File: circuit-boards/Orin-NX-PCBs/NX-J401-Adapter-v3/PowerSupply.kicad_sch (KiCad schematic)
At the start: 23 parts, among them Q4 CSD16322Q5, Q5 SI4483ADY-T1-GE3, U2 LM3478MA

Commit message: Updated diff pairs and power supply layout
Signed-off-by: Scott <sgberman1@gmail.com>
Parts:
- renumbered C5 to C4, C13 to C5, C6 to C8, D3 to D1, R2 to R1, R8 to R4, R5 to R7, R6 to R8, U2 to U1
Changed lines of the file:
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@@
 	(title_block
 		(title "NX J401 Adapter")
-		(date "2024-08-05")
+		(date "2024-08-10")
 		(rev "3")
 		(company "971 Spartan Robotics")
@@
 		(on_board yes)
 		(dnp no)
-		(property "Reference" "R5"
+		(property "Reference" "R7"
 			(at 95.25 105.41 0)
 			(effects
@@
 			(project "NX-J401-Adapter"
 				(path "/cc31ce4b-09ab-4aea-a1d3-ed84696ba658/584f7d71-5922-4ce5-8f88-d664ca9e2a8c"
-					(reference "R5")
+					(reference "R7")
 					(unit 1)
 				)
@@
 			(project "NX-J401-Adapter"
 				(path "/cc31ce4b-09ab-4aea-a1d3-ed84696ba658/584f7d71-5922-4ce5-8f88-d664ca9e2a8c"
-					(reference "R9")
+					(reference "R6")
 					(unit 1)
 				)
@@
 			(project "NX-J401-Adapter"
 				(path "/cc31ce4b-09ab-4aea-a1d3-ed84696ba658/584f7d71-5922-4ce5-8f88-d664ca9e2a8c"
-					(reference "C7")
+					(reference "C3")
 					(unit 1)
 				)
@@
 			(project "NX-J401-Adapter"
 				(path "/cc31ce4b-09ab-4aea-a1d3-ed84696ba658/584f7d71-5922-4ce5-8f88-d664ca9e2a8c"
-					(reference "R3")
+					(reference "R5")
 					(unit 1)
 				)
@@
 			(project "NX-J401-Adapter"
 				(path "/cc31ce4b-09ab-4aea-a1d3-ed84696ba658/584f7d71-5922-4ce5-8f88-d664ca9e2a8c"
-					(reference "C11")
+					(reference "C7")
 					(unit 1)
 				)
@@
 			(project "NX-J401-Adapter"
 				(path "/cc31ce4b-09ab-4aea-a1d3-ed84696ba658/584f7d71-5922-4ce5-8f88-d664ca9e2a8c"
-					(reference "R4")
+					(reference "R2")
 					(unit 1)
 				)
@@
 		(on_board yes)
 		(dnp no)
-		(property "Reference" "C5"
+		(property "Reference" "C4"
 			(at 149.86 97.79 0)
 			(effects
@@
 			(project "NX-J401-Adapter"
 				(path "/cc31ce4b-09ab-4aea-a1d3-ed84696ba658/584f7d71-5922-4ce5-8f88-d664ca9e2a8c"
-					(reference "C5")
+					(reference "C4")
 					(unit 1)
 				)
@@
 		(dnp no)
 		(fields_autoplaced yes)
-		(property "Reference" "C13"
+		(property "Reference" "C5"
 			(at 130.81 98.425 0)
 			(effects
@@
 			(project "NX-J401-Adapter"
 				(path "/cc31ce4b-09ab-4aea-a1d3-ed84696ba658/584f7d71-5922-4ce5-8f88-d664ca9e2a8c"
-					(reference "C13")
+					(reference "C5")
 					(unit 1)
 				)
@@
 			(project "NX-J401-Adapter"
 				(path "/cc31ce4b-09ab-4aea-a1d3-ed84696ba658/584f7d71-5922-4ce5-8f88-d664ca9e2a8c"
-					(reference "D5")
+					(reference "D2")
 					(unit 1)
 				)
@@
 		(on_board yes)
 		(dnp no)
-		(property "Reference" "R8"
+		(property "Reference" "R4"
 			(at 284.48 116.84 0)
 			(effects
@@
 			(project "NX-J401-Adapter"
 				(path "/cc31ce4b-09ab-4aea-a1d3-ed84696ba658/584f7d71-5922-4ce5-8f88-d664ca9e2a8c"
-					(reference "R8")
+					(reference "R4")
 					(unit 1)
 				)
@@
 			(project "NX-J401-Adapter"
 				(path "/cc31ce4b-09ab-4aea-a1d3-ed84696ba658/584f7d71-5922-4ce5-8f88-d664ca9e2a8c"
-					(reference "R7")
+					(reference "R3")
 					(unit 1)
 				)
@@
 		(on_board yes)
 		(dnp no)
-		(property "Reference" "C6"
+		(property "Reference" "C8"
 			(at 69.85 97.79 0)
 			(effects
@@
 			(project "NX-J401-Adapter"
 				(path "/cc31ce4b-09ab-4aea-a1d3-ed84696ba658/584f7d71-5922-4ce5-8f88-d664ca9e2a8c"
-					(reference "C6")
+					(reference "C8")
 					(unit 1)
 				)
@@
 			(project "NX-J401-Adapter"
 				(path "/cc31ce4b-09ab-4aea-a1d3-ed84696ba658/584f7d71-5922-4ce5-8f88-d664ca9e2a8c"
-					(reference "L2")
+					(reference "L1")
 					(unit 1)
 				)
@@
 		(on_board yes)
 		(dnp no)
-		(property "Reference" "R2"
+		(property "Reference" "R1"
 			(at 254 115.57 0)
 			(effects
@@
 			(project "NX-J401-Adapter"
 				(path "/cc31ce4b-09ab-4aea-a1d3-ed84696ba658/584f7d71-5922-4ce5-8f88-d664ca9e2a8c"
-					(reference "R2")
+					(reference "R1")
 					(unit 1)
 				)
@@
 		(on_board yes)
 		(dnp yes)
-		(property "Reference" "R6"
+		(property "Reference" "R8"
 			(at 98.298 84.836 90)
 			(effects
@@
 			(project "NX-J401-Adapter"
 				(path "/cc31ce4b-09ab-4aea-a1d3-ed84696ba658/584f7d71-5922-4ce5-8f88-d664ca9e2a8c"
-					(reference "R6")
+					(reference "R8")
 					(unit 1)
 				)
@@
 		(dnp no)
 		(fields_autoplaced yes)
-		(property "Reference" "D3"
+		(property "Reference" "D1"
 			(at 267.081 64.77 0)
 			(effects
@@
 			(project "NX-J401-Adapter"
 				(path "/cc31ce4b-09ab-4aea-a1d3-ed84696ba658/584f7d71-5922-4ce5-8f88-d664ca9e2a8c"
-					(reference "D3")
+					(reference "D1")
 					(unit 1)
 				)
@@
 		(dnp no)
 		(fields_autoplaced yes)
-		(property "Reference" "U2"
+		(property "Reference" "U1"
 			(at 210.82 77.47 0)
 			(effects
@@
 			(project "NX-J401-Adapter"
 				(path "/cc31ce4b-09ab-4aea-a1d3-ed84696ba658/584f7d71-5922-4ce5-8f88-d664ca9e2a8c"
-					(reference "U2")
+					(reference "U1")
 					(unit 1)
 				)
@@
 			(project "NX-J401-Adapter"
 				(path "/cc31ce4b-09ab-4aea-a1d3-ed84696ba658/584f7d71-5922-4ce5-8f88-d664ca9e2a8c"
-					(reference "C12")
+					(reference "C6")
 					(unit 1)
 				)
@@
 			(project "NX-J401-Adapter"
 				(path "/cc31ce4b-09ab-4aea-a1d3-ed84696ba658/584f7d71-5922-4ce5-8f88-d664ca9e2a8c"
-					(reference "D4")
+					(reference "D3")
 					(unit 1)
 				)

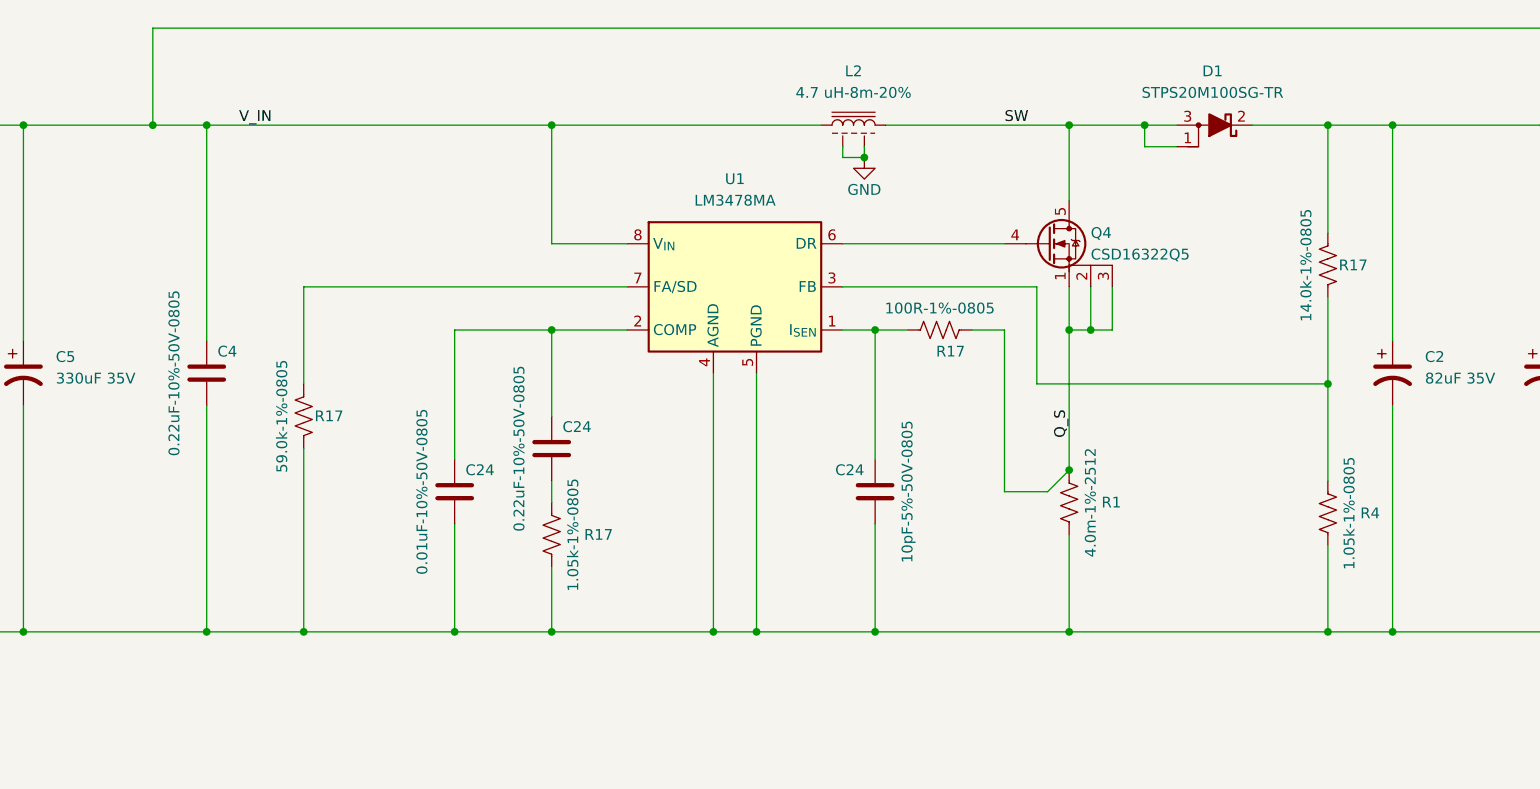
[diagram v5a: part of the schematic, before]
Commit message: minor update to boost converter layout
Signed-off-by: Scott Berman <scott.berman@bluerivertech.com>
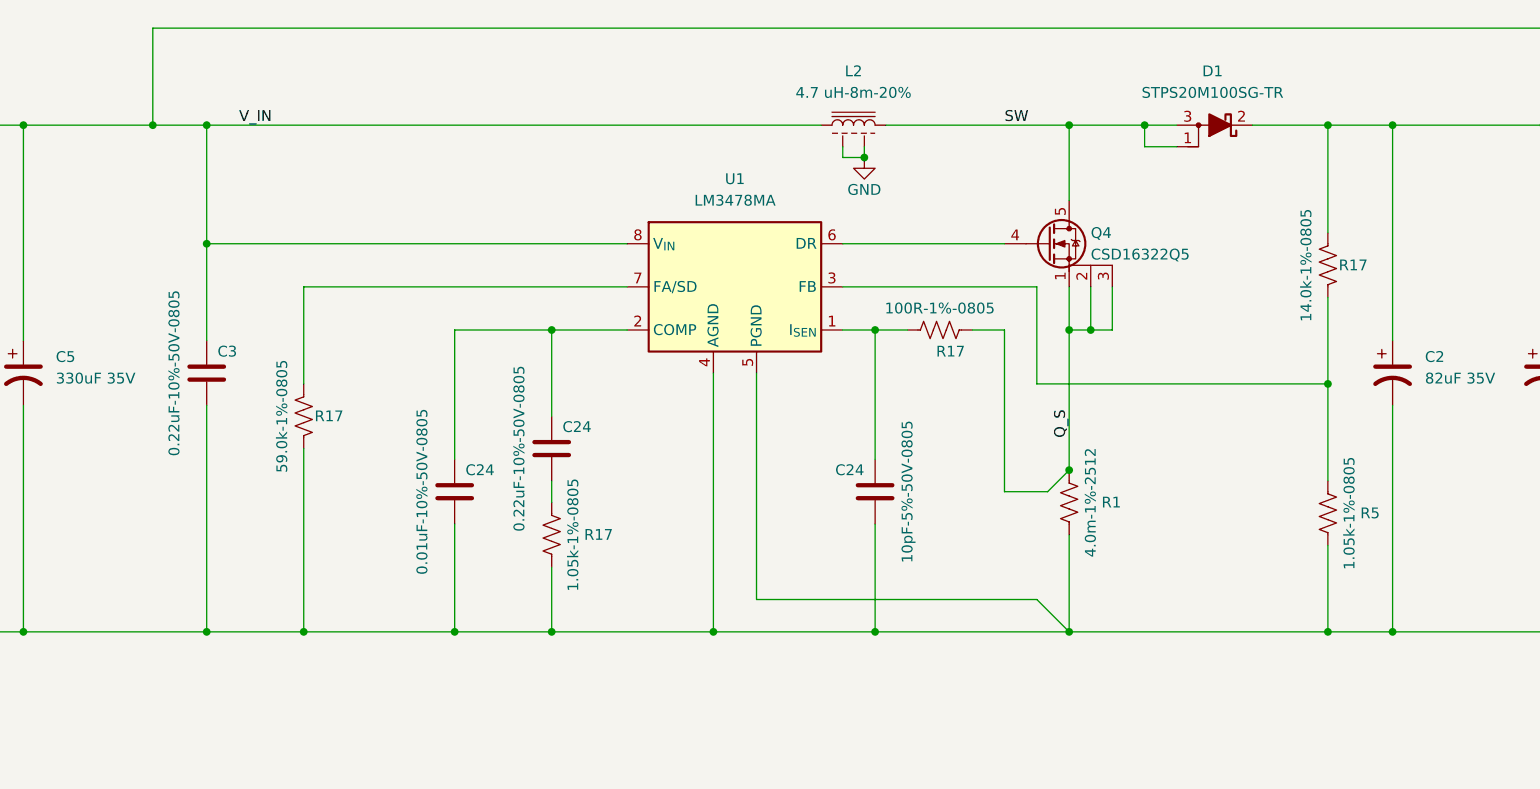
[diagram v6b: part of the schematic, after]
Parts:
- renumbered C4 to C3, R4 to R5
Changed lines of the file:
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@@
 	)
 	(junction
+		(at 148.59 71.12)
+		(diameter 0)
+		(color 0 0 0 0)
+	)
+	(junction
 		(at 99.06 71.12)
 		(diameter 0)
@@
 	)
 	(junction
-		(at 189.23 71.12)
-		(diameter 0)
-		(color 0 0 0 0)
-	)
-	(junction
 		(at 189.23 130.81)
 		(diameter 0)
@@
 	)
 	(junction
-		(at 213.36 130.81)
-		(diameter 0)
-		(color 0 0 0 0)
-	)
-	(junction
 		(at 100.33 71.12)
 		(diameter 0)
@@
 	)
 	(junction
+		(at 148.59 85.09)
+		(diameter 0)
+		(color 0 0 0 0)
+	)
+	(junction
 		(at 160.02 130.81)
 		(diameter 0)
@@
 	)
 	(junction
-		(at 148.59 71.12)
-		(diameter 0)
-		(color 0 0 0 0)
-	)
-	(junction
 		(at 250.19 130.81)
 		(diameter 0)
@@
 	(wire
 		(pts
-			(xy 213.36 100.33) (xy 213.36 130.81)
-		)
-		(stroke
-			(width 0)
-			(type default)
-		)
-	)
-	(wire
-		(pts
 			(xy 252.73 95.25) (xy 250.19 95.25)
 		)
@@
 	(wire
 		(pts
-			(xy 148.59 71.12) (xy 142.24 71.12)
-		)
-		(stroke
-			(width 0)
-			(type default)
-		)
-	)
-	(wire
-		(pts
-			(xy 148.59 96.52) (xy 148.59 71.12)
+			(xy 142.24 71.12) (xy 148.59 71.12)
 		)
 		(stroke
@@
 	(wire
 		(pts
-			(xy 189.23 71.12) (xy 189.23 85.09)
-		)
-		(stroke
-			(width 0)
-			(type default)
-		)
-	)
-	(wire
-		(pts
 			(xy 71.12 130.81) (xy 91.44 130.81)
 		)
@@
 	(wire
 		(pts
-			(xy 208.28 130.81) (xy 213.36 130.81)
+			(xy 255.27 90.17) (xy 255.27 95.25)
 		)
 		(stroke
@@
 	(wire
 		(pts
-			(xy 255.27 90.17) (xy 255.27 95.25)
+			(xy 213.36 100.33) (xy 213.36 127)
 		)
 		(stroke
@@
 	(wire
 		(pts
-			(xy 213.36 130.81) (xy 227.33 130.81)
+			(xy 208.28 130.81) (xy 227.33 130.81)
 		)
 		(stroke
@@
 	(wire
 		(pts
-			(xy 189.23 71.12) (xy 220.98 71.12)
-		)
-		(stroke
-			(width 0)
-			(type default)
-		)
-	)
-	(wire
-		(pts
 			(xy 177.8 95.25) (xy 189.23 95.25)
 		)
@@
 	(wire
 		(pts
+			(xy 148.59 85.09) (xy 198.12 85.09)
+		)
+		(stroke
+			(width 0)
+			(type default)
+		)
+	)
+	(wire
+		(pts
 			(xy 148.59 130.81) (xy 127 130.81)
 		)
@@
 	(wire
 		(pts
+			(xy 148.59 71.12) (xy 220.98 71.12)
+		)
+		(stroke
+			(width 0)
+			(type default)
+		)
+	)
+	(wire
+		(pts
 			(xy 100.33 71.12) (xy 100.33 78.74)
 		)
@@
 	(wire
 		(pts
-			(xy 148.59 71.12) (xy 189.23 71.12)
+			(xy 213.36 127) (xy 246.38 127)
 		)
 		(stroke
@@
 	(wire
 		(pts
-			(xy 142.24 71.12) (xy 127 71.12)
+			(xy 250.19 130.81) (xy 246.38 127)
 		)
 		(stroke
@@
 	(wire
 		(pts
-			(xy 83.82 66.04) (xy 83.82 68.58)
+			(xy 142.24 71.12) (xy 127 71.12)
 		)
 		(stroke
@@
 	(wire
 		(pts
-			(xy 189.23 85.09) (xy 198.12 85.09)
+			(xy 83.82 66.04) (xy 83.82 68.58)
 		)
 		(stroke
@@
 	(wire
 		(pts
+			(xy 148.59 85.09) (xy 148.59 96.52)
+		)
+		(stroke
+			(width 0)
+			(type default)
+		)
+	)
+	(wire
+		(pts
+			(xy 148.59 85.09) (xy 148.59 71.12)
+		)
+		(stroke
+			(width 0)
+			(type default)
+		)
+	)
+	(wire
+		(pts
 			(xy 306.07 71.12) (xy 306.07 96.52)
 		)
@@
 			(project "NX-J401-Adapter"
 				(path "/cc31ce4b-09ab-4aea-a1d3-ed84696ba658/584f7d71-5922-4ce5-8f88-d664ca9e2a8c"
-					(reference "C3")
+					(reference "C4")
 					(unit 1)
 				)
@@
 			(project "NX-J401-Adapter"
 				(path "/cc31ce4b-09ab-4aea-a1d3-ed84696ba658/584f7d71-5922-4ce5-8f88-d664ca9e2a8c"
-					(reference "R5")
+					(reference "R4")
 					(unit 1)
 				)
@@
 			(project "NX-J401-Adapter"
 				(path "/cc31ce4b-09ab-4aea-a1d3-ed84696ba658/584f7d71-5922-4ce5-8f88-d664ca9e2a8c"
-					(reference "R2")
+					(reference "R3")
 					(unit 1)
 				)
@@
 		(on_board yes)
 		(dnp no)
-		(property "Reference" "C4"
+		(property "Reference" "C3"
 			(at 149.86 97.79 0)
 			(effects
@@
 			(project "NX-J401-Adapter"
 				(path "/cc31ce4b-09ab-4aea-a1d3-ed84696ba658/584f7d71-5922-4ce5-8f88-d664ca9e2a8c"
-					(reference "C4")
+					(reference "C3")
 					(unit 1)
 				)
@@
 		(on_board yes)
 		(dnp no)
-		(property "Reference" "R4"
+		(property "Reference" "R5"
 			(at 284.48 116.84 0)
 			(effects
@@
 			(project "NX-J401-Adapter"
 				(path "/cc31ce4b-09ab-4aea-a1d3-ed84696ba658/584f7d71-5922-4ce5-8f88-d664ca9e2a8c"
-					(reference "R4")
+					(reference "R5")
 					(unit 1)
 				)
@@
 			(project "NX-J401-Adapter"
 				(path "/cc31ce4b-09ab-4aea-a1d3-ed84696ba658/584f7d71-5922-4ce5-8f88-d664ca9e2a8c"
-					(reference "R3")
+					(reference "R2")
 					(unit 1)
 				)
